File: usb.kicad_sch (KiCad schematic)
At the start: 29 parts, among them J3 USB4105-GF-A, U11 TPD4E05U06QDQARQ1, U5 FT230X, U8 NCP730BMT330

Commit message: Layout cleanup, silk
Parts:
- TP15, TP16: footprint JetsonCarrier:TP_SMD_0.75mm -> TestPoint:TestPoint_Pad_D1.0mm
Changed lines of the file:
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@@
 			)
 		)
-		(property "Footprint" "JetsonCarrier:TP_SMD_0.75mm"
+		(property "Footprint" "TestPoint:TestPoint_Pad_D1.0mm"
 			(at 133.35 161.29 0)
 			(hide yes)
@@
 			)
 		)
-		(property "Footprint" "JetsonCarrier:TP_SMD_0.75mm"
+		(property "Footprint" "TestPoint:TestPoint_Pad_D1.0mm"
 			(at 133.35 168.91 0)
 			(hide yes)

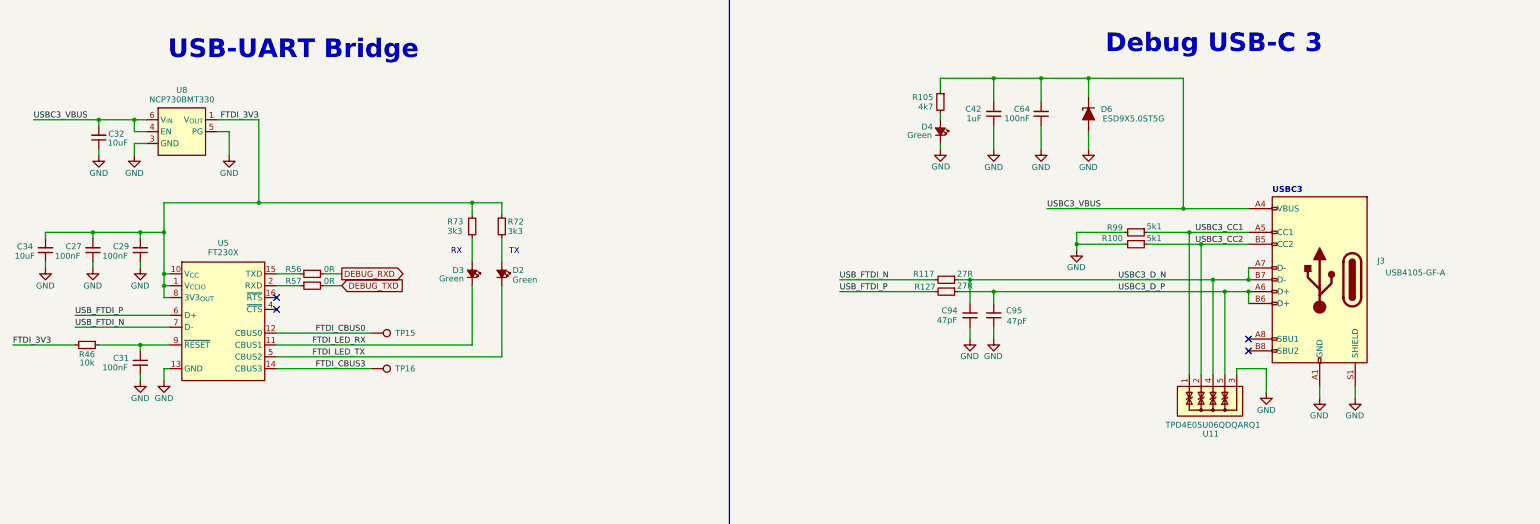
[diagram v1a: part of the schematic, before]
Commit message: route all diff pairs, length tuning
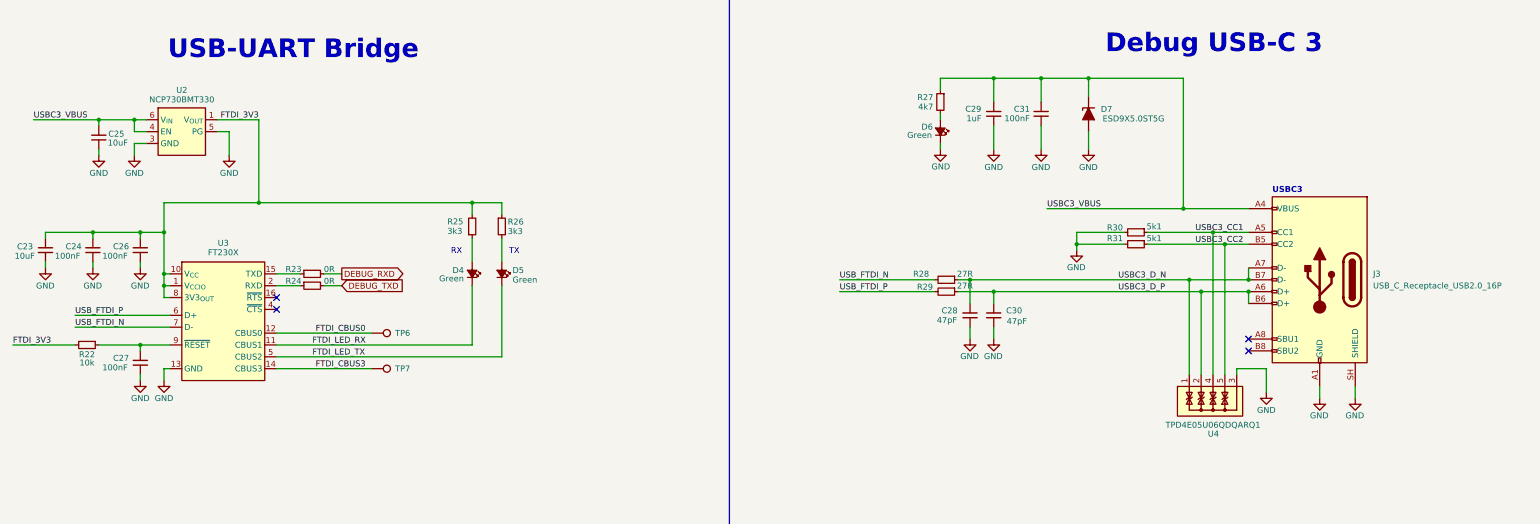
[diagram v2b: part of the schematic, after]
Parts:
- J3: value USB4105-GF-A -> USB_C_Receptacle_USB2.0_16P; Author Antmicro -> (none); License Apache-2.0 -> (none); MPN USB4105-GF-A -> (none); Manufacturer GCT -> (none)
- R30: renamed from R99; footprint Resistor_SMD:R_0402_1005Metric -> Resistor_SMD:R_0603_1608Metric
- R31: renamed from R100; footprint Resistor_SMD:R_0402_1005Metric -> Resistor_SMD:R_0603_1608Metric
- renumbered C34 to C23, C27 to C24, C32 to C25, C29 to C26, C31 to C27, C94 to C28, C42 to C29, C95 to C30, C64 to C31, D3 to D4, D2 to D5, D4 to D6, D6 to D7, R46 to R22, R56 to R23, R57 to R24, R73 to R25, R72 to R26, R105 to R27, R117 to R28, R127 to R29, TP15 to TP6, TP16 to TP7, U8 to U2, U5 to U3, U11 to U4
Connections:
- net GND: now also J3.SH (SHIELD); no longer J3.S1 (SHIELD)
- net USBC3_CC1: now also U4.4, U4.7; no longer U4.1, U4.10
- net USBC3_CC2: now also U4.5, U4.6; no longer U4.2, U4.9
- net USBC3_D_N: now also U4.1, U4.10; no longer U4.4, U4.7
- net USBC3_D_P: now also U4.2, U4.9; no longer U4.5, U4.6

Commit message: additional cleanup
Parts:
- U3: footprint JetsonCarrier:QFN-16-1EP_4x4mm_P0.65mm -> Package_DFN_QFN:QFN-16-1EP_4x4mm_P0.65mm_EP2.1x2.1mm
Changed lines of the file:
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@@
 			)
 		)
-		(property "Footprint" "JetsonCarrier:QFN-16-1EP_4x4mm_P0.65mm"
+		(property "Footprint" "Package_DFN_QFN:QFN-16-1EP_4x4mm_P0.65mm_EP2.1x2.1mm"
 			(at 129.54 156.21 0)
 			(hide yes)

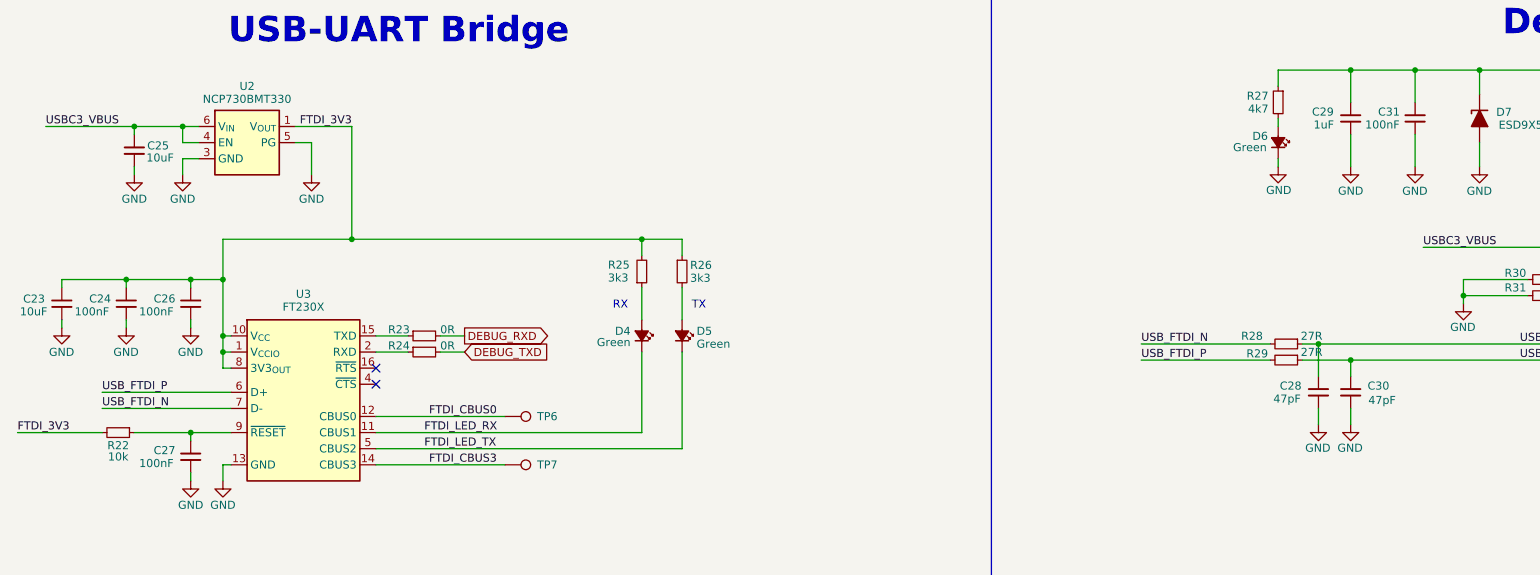
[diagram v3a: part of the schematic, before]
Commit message: Replace current monitor w/ INA226 (addr = 0x42)
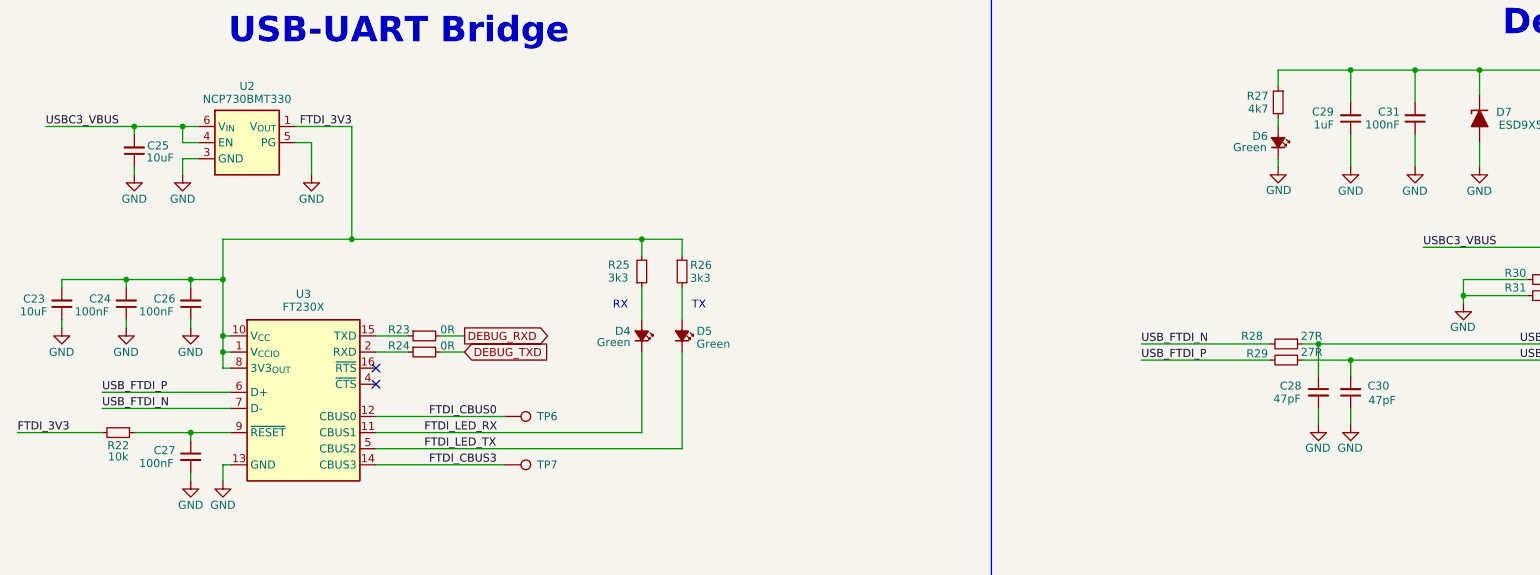
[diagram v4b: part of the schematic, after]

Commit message: Final BOM changes, gerbers
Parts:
- C23, C25: LCSC (none) -> C96446
- C24, C26, C27, C31: LCSC (none) -> C14663
- C28, C30: LCSC (none) -> C1567
- C29: LCSC (none) -> C15849
- D4, D5: LCSC (none) -> C2290
- D6: LCSC (none) -> C12065
- D7: LCSC (none) -> C87910
- J3: LCSC (none) -> C3020560
- R22: LCSC (none) -> C25804
- R23, R24: LCSC (none) -> C17168
- R25, R26: LCSC (none) -> C22978
- R27: LCSC (none) -> C23162
- R28, R29: LCSC (none) -> C227752
- R30, R31: LCSC (none) -> C23186
- U2: LCSC (none) -> C892821
- U3: LCSC (none) -> C128629
- U4: LCSC (none) -> C81353
